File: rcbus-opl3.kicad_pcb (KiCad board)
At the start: 2 copper layers, 100 x 50 mm, 35 parts, among them CON1 3.5mm jack, P1 RC2014 BUS, U1 74HCT688, U2 YMF262, U3 YAC512, U4 TL074, Y1 14.3181MHz

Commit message: add cc logos and some tidyup
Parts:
- added REF**: Symbol_CreativeCommons_CopperTop_Type2_Big, Symbol:Symbol_CreativeCommons_CopperTop_Type2_Big, F.Cu at (53.0, 96.5)
- added REF**: Symbol_CC-Attribution_Silk_Small, electrified:Symbol_CC-Attribution_Silk_Small, B.Cu at (97.5, 159.0)
- added REF**: Symbol_CC-ShareAlike_Silk_Small, electrified:Symbol_CC-ShareAlike_Silk_Small, B.Cu at (91.5, 159.0)
- added REF**: Symbol_CreativeCommons_Silk_Type2_Small, electrified:Symbol_CreativeCommons_Silk_Type2_Small, B.Cu at (103.5, 159.0)
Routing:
- net /AUDIO_CH1: track 20.1 -> 20.8 mm
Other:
- board text added: "CC BY-SA https://creativecommons.org"

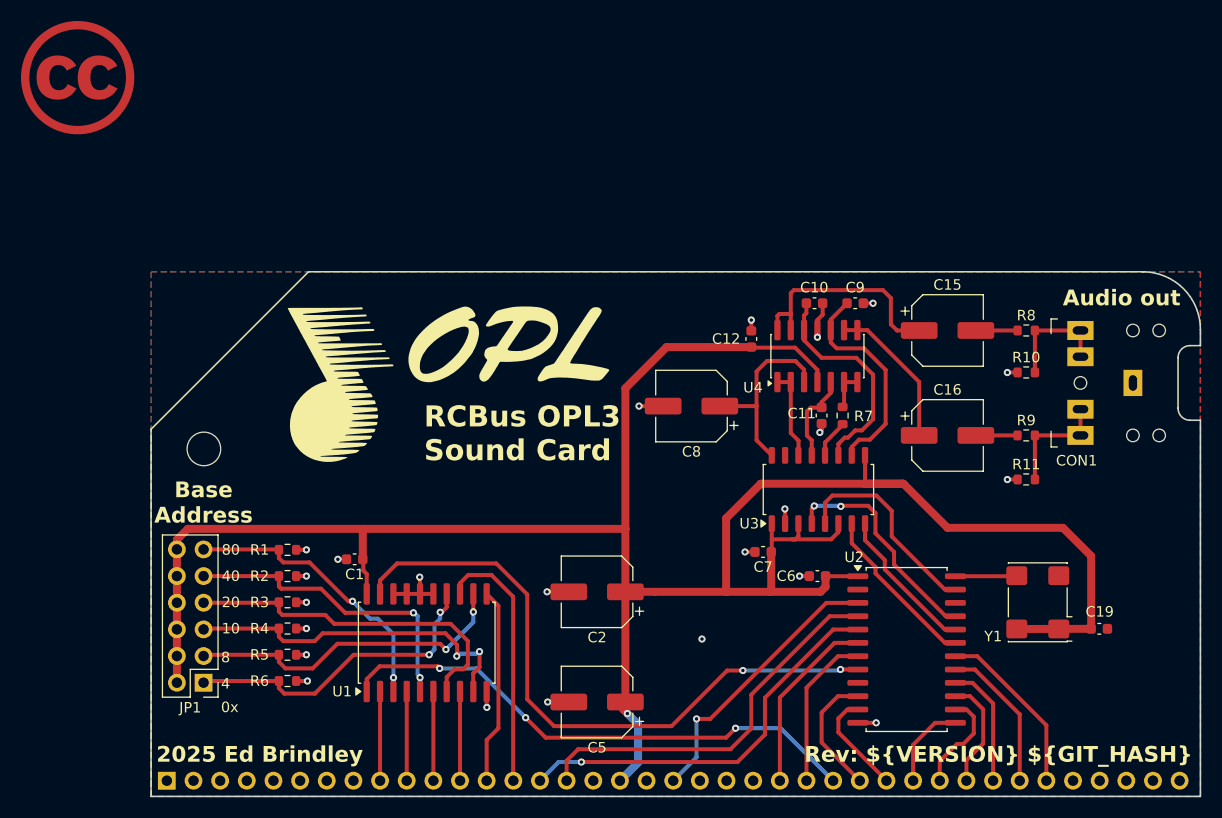
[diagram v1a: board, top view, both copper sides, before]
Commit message: add stitching vias
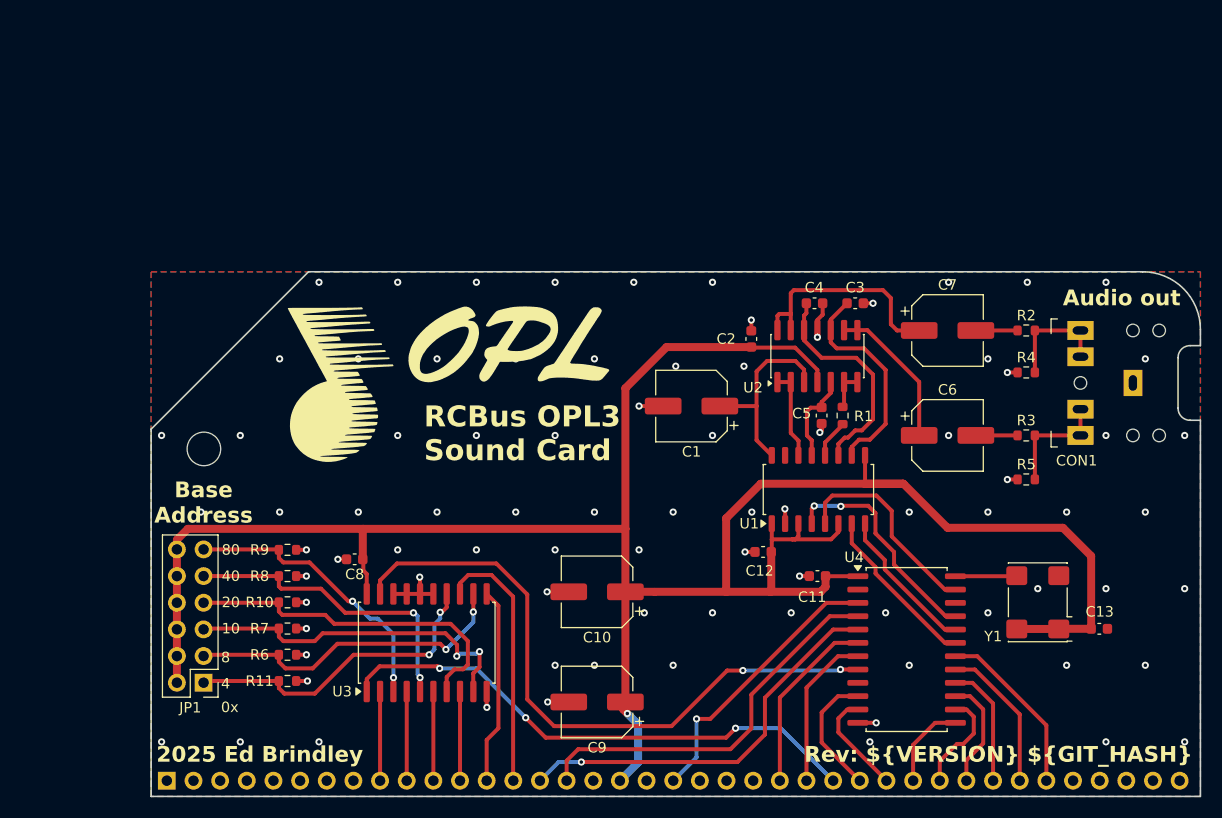
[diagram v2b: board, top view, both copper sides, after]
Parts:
- removed the REF** at (53.0, 96.5)
- C10: renamed from C2; value 10uf -> 10uF
- C3: renamed from C9; value 2.7nf -> 2.7nF
- C4: renamed from C10; value 2.7nf -> 2.7nF
- C5: renamed from C11; value 68pf -> 68pF
- C6: renamed from C16; value 10uf -> 10uF
- C7: renamed from C15; value 10uf -> 10uF
- renumbered C8 to C1, C6 to C11, C7 to C12, C19 to C13, C12 to C2, C1 to C8, C5 to C9, R7 to R1, R3 to R10, R6 to R11, R8 to R2, R9 to R3, R10 to R4, R11 to R5, R5 to R6, R4 to R7, R2 to R8, R1 to R9, U3 to U1, U4 to U2, U1 to U3, U2 to U4
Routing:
- net GND: vias 23 -> 86

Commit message: more tidyup
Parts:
- renumbered C6 to C2, C4 to C3, C3 to C4, C2 to C5, C5 to C6, REF** to G3, REF** to G4, REF** to G5, R4 to R2, R2 to R3, R3 to R4, R7 to R6, R6 to R7, U2 to U1, U1 to U2
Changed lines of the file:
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@@
 		(descr "Capacitor SMD 0603 (1608 Metric), square (rectangular) end terminal, IPC-7351 nominal, (Body size source: IPC-SM-782 page 76, https://www.pcb-3d.com/wordpress/wp-content/uploads/ipc-sm-782a_amendment_1_and_2.pdf), generated with kicad-footprint-generator")
 		(tags "capacitor")
-		(property "Reference" "C5"
+		(property "Reference" "C6"
 			(at -0.2 1.9 0)
 			(layer "F.SilkS")
@@
 		(descr "Capacitor SMD 0603 (1608 Metric), square (rectangular) end terminal, IPC-7351 nominal, (Body size source: IPC-SM-782 page 76, https://www.pcb-3d.com/wordpress/wp-content/uploads/ipc-sm-782a_amendment_1_and_2.pdf), generated with kicad-footprint-generator")
 		(tags "capacitor")
-		(property "Reference" "C2"
+		(property "Reference" "C5"
 			(at 0 -2.4 0)
 			(layer "F.SilkS")
@@
 		(descr "SOP, 16 Pin (https://toshiba.semicon-storage.com/info/docget.jsp?did=12855&prodName=TLP290-4), generated with kicad-footprint-generator ipc_gullwing_generator.py")
 		(tags "SOP SO")
-		(property "Reference" "U1"
+		(property "Reference" "U2"
 			(at -3.25 -6.595 0)
 			(layer "F.SilkS")
@@
 		(descr "Capacitor SMD 0603 (1608 Metric), square (rectangular) end terminal, IPC-7351 nominal, (Body size source: IPC-SM-782 page 76, https://www.pcb-3d.com/wordpress/wp-content/uploads/ipc-sm-782a_amendment_1_and_2.pdf), generated with kicad-footprint-generator")
 		(tags "capacitor")
-		(property "Reference" "C3"
+		(property "Reference" "C4"
 			(at 0 -1.5 180)
 			(layer "F.SilkS")
@@
 		(descr "Resistor SMD 0603 (1608 Metric), square (rectangular) end terminal, IPC-7351 nominal, (Body size source: IPC-SM-782 page 72, https://www.pcb-3d.com/wordpress/wp-content/uploads/ipc-sm-782a_amendment_1_and_2.pdf), generated with kicad-footprint-generator")
 		(tags "resistor")
-		(property "Reference" "R6"
+		(property "Reference" "R7"
 			(at -2.6625 0 0)
 			(layer "F.SilkS")
@@
 		(descr "Resistor SMD 0603 (1608 Metric), square (rectangular) end terminal, IPC-7351 nominal, (Body size source: IPC-SM-782 page 72, https://www.pcb-3d.com/wordpress/wp-content/uploads/ipc-sm-782a_amendment_1_and_2.pdf), generated with kicad-footprint-generator")
 		(tags "resistor")
-		(property "Reference" "R2"
+		(property "Reference" "R3"
 			(at 0 -1.43 0)
 			(layer "F.SilkS")
@@
 		(descr "Resistor SMD 0603 (1608 Metric), square (rectangular) end terminal, IPC-7351 nominal, (Body size source: IPC-SM-782 page 72, https://www.pcb-3d.com/wordpress/wp-content/uploads/ipc-sm-782a_amendment_1_and_2.pdf), generated with kicad-footprint-generator")
 		(tags "resistor")
-		(property "Reference" "R3"
+		(property "Reference" "R4"
 			(at 0 -1.43 0)
 			(layer "F.SilkS")
@@
 		(descr "Capacitor SMD 0603 (1608 Metric), square (rectangular) end terminal, IPC-7351 nominal, (Body size source: IPC-SM-782 page 76, https://www.pcb-3d.com/wordpress/wp-content/uploads/ipc-sm-782a_amendment_1_and_2.pdf), generated with kicad-footprint-generator")
 		(tags "capacitor")
-		(property "Reference" "C4"
+		(property "Reference" "C3"
 			(at -0.025 -1.5 180)
 			(layer "F.SilkS")
@@
 		(descr "SOIC, 14 Pin (JEDEC MS-012AB, https://www.analog.com/media/en/package-pcb-resources/package/pkg_pdf/soic_narrow-r/r_14.pdf), generated with kicad-footprint-generator ipc_gullwing_generator.py")
 		(tags "SOIC SO")
-		(property "Reference" "U2"
+		(property "Reference" "U1"
 			(at -3 -6.1375 0)
 			(layer "F.SilkS")
@@
 		(descr "SMD capacitor, aluminum electrolytic, Nichicon, 6.3x5.8mm")
 		(tags "capacitor electrolytic")
-		(property "Reference" "C6"
+		(property "Reference" "C2"
 			(at 0 -4.35 0)
 			(layer "F.SilkS")
@@
 		(descr "Resistor SMD 0603 (1608 Metric), square (rectangular) end terminal, IPC-7351 nominal, (Body size source: IPC-SM-782 page 72, https://www.pcb-3d.com/wordpress/wp-content/uploads/ipc-sm-782a_amendment_1_and_2.pdf), generated with kicad-footprint-generator")
 		(tags "resistor")
-		(property "Reference" "R7"
+		(property "Reference" "R6"
 			(at -2.6625 0 0)
 			(layer "F.SilkS")
@@
 		(descr "Resistor SMD 0603 (1608 Metric), square (rectangular) end terminal, IPC-7351 nominal, (Body size source: IPC-SM-782 page 72, https://www.pcb-3d.com/wordpress/wp-content/uploads/ipc-sm-782a_amendment_1_and_2.pdf), generated with kicad-footprint-generator")
 		(tags "resistor")
-		(property "Reference" "R4"
+		(property "Reference" "R2"
 			(at 0 -1.43 0)
 			(layer "F.SilkS")
@@
 		(at 97.5 159 180)
 		(descr "Creative Commons symbol, CC-BY, copper layer, 5mm")
-		(property "Reference" "REF**"
+		(property "Reference" "G4"
 			(at 0 4 0)
 			(layer "B.SilkS")
@@
 		(descr "Creative Commons symbol, CC-SA, copper layer, 5mm")
 		(tags "share-alike license graphic")
-		(property "Reference" "REF**"
+		(property "Reference" "G5"
 			(at 0 4 0)
 			(layer "B.SilkS")
@@
 		(descr "Creative Commons symbol, CC, copper layer, 5mm")
 		(tags "license graphic")
-		(property "Reference" "REF**"
+		(property "Reference" "G3"
 			(at 0 3.5 0)
 			(layer "B.SilkS")
@@
 	)
 	(segment
-		(start 91.98 159.62)
-		(end 91.98 163.5)
+		(start 92.6 145.7)
+		(end 93.1 146.2)
 		(width 0.381)
 		(layer "F.Cu")
@@
 	)
 	(segment
-		(start 93.1 146.82)
-		(end 93.1 158.5)
+		(start 91.98 145.7)
+		(end 92.6 145.7)
 		(width 0.381)
 		(layer "F.Cu")
@@
 	)
 	(segment
-		(start 91.98 145.7)
-		(end 93.1 146.82)
+		(start 91.98 159.62)
+		(end 91.98 163.5)
+		(width 0.381)
+		(layer "F.Cu")
+		(net 14)
+	)
+	(segment
+		(start 93.1 146.2)
+		(end 93.1 158.5)
 		(width 0.381)
 		(layer "F.Cu")
@@
 		(polygon
 			(pts
-				(xy 80.1 140.5) (xy 80.4 146) (xy 93 146) (xy 92.8 153.975) (xy 95.7 158.5) (xy 105.2 158.5) (xy 105.2 164.7)
-				(xy 81.8 164.639114) (xy 81.8 154.425404) (xy 79.6 154.4) (xy 79.6 151.399999) (xy 75.540613 155.059387)
-				(xy 72.4 155) (xy 72.398643 154.084962) (xy 67.08 154) (xy 67 140.5)
+				(xy 80.1 140.5) (xy 80.4 146) (xy 83.5 143) (xy 92.8 143) (xy 92.8 153.975) (xy 95.7 158.5) (xy 105.2 158.5)
+				(xy 105.2 164.7) (xy 81.8 164.639114) (xy 81.8 154.425404) (xy 79.6 154.4) (xy 79.6 151.399999)
+				(xy 75.540613 155.059387) (xy 72.4 155) (xy 72.398643 154.084962) (xy 67.08 154) (xy 67 140.5)
 			)
 		)

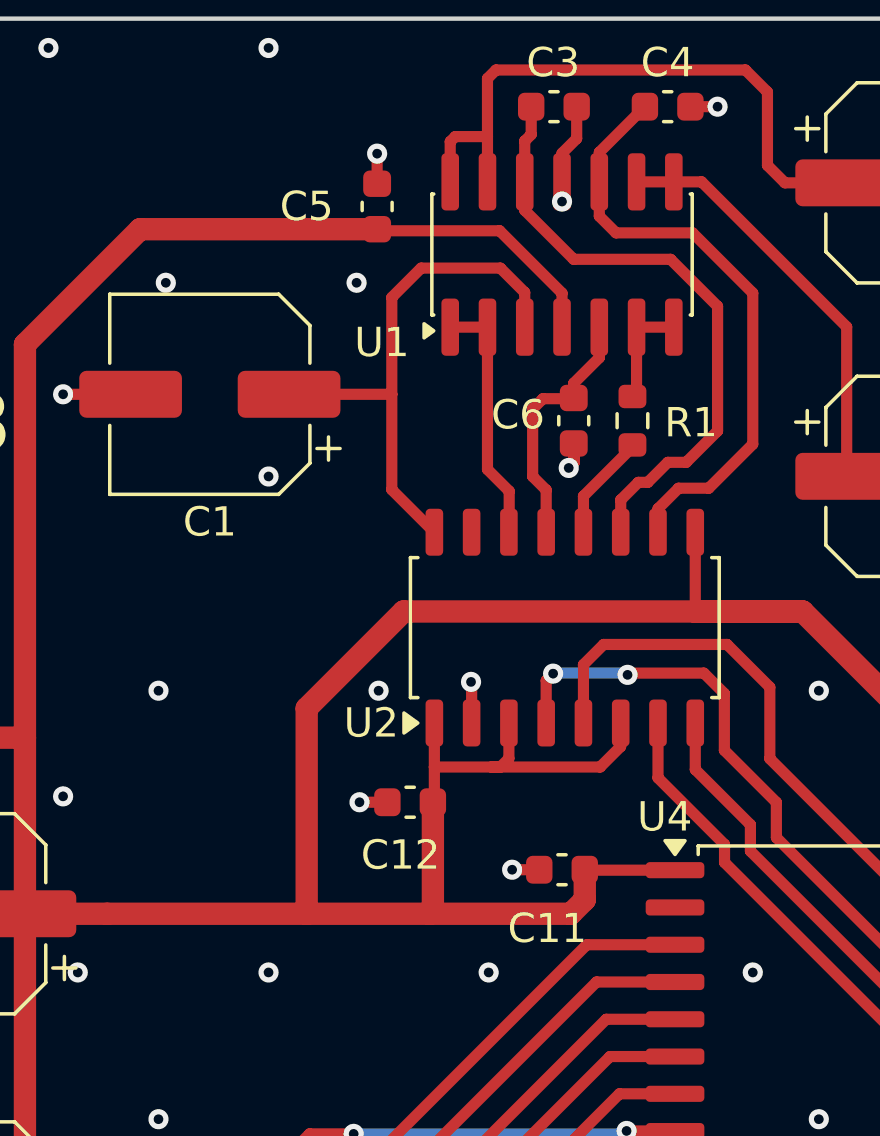
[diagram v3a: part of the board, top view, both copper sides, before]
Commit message: tidy up text
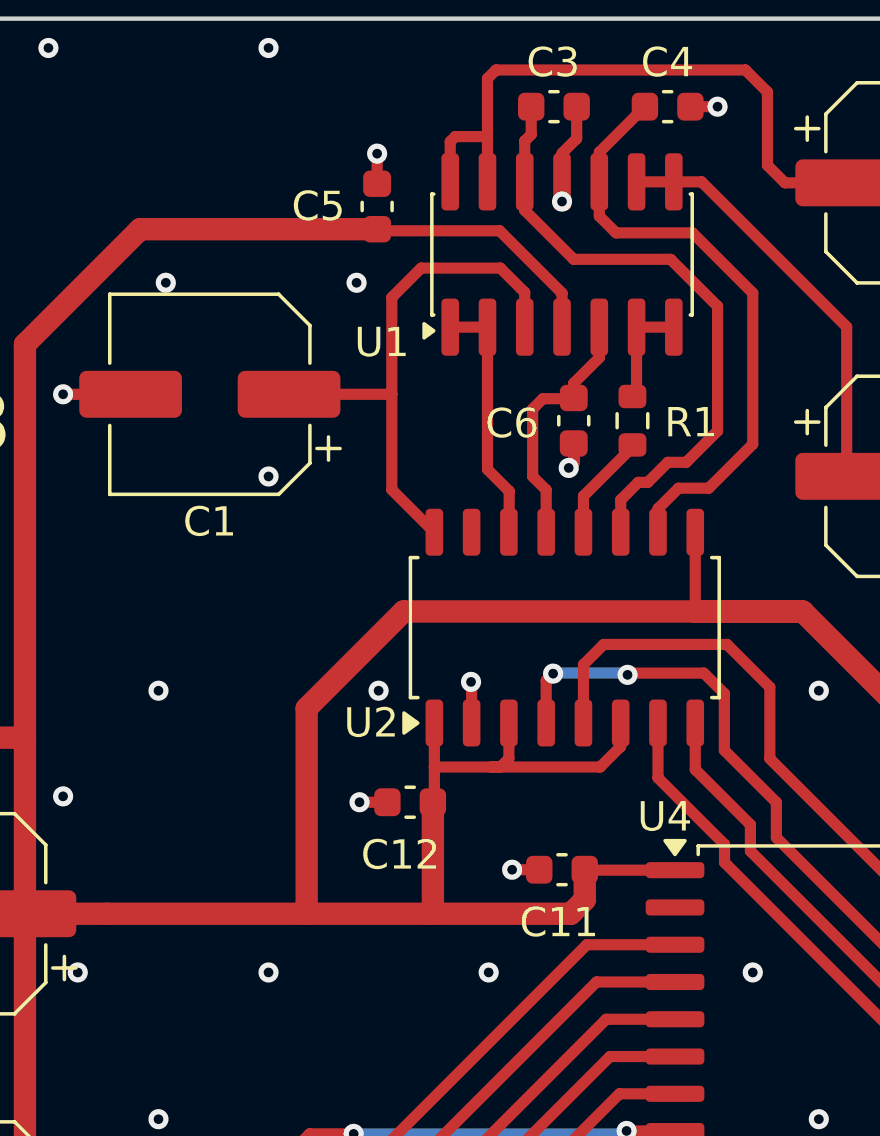
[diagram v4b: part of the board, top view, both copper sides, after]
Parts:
- moved G3 1.00 mm to (104.5, 159.0)
- moved G4 1.00 mm to (98.5, 159.0)
- moved G5 1.00 mm to (92.5, 159.0)
